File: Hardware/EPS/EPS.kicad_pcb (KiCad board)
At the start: 4 copper layers, 85 x 85 mm, 111 parts, among them J1001 Conn_01x02, J1101 Conn_01x02, J201 Conn_ARM_JTAG_SWD_10, J301 Conn_02x02_Counter_Clockwise, J401 USB_C_Receptacle_PowerOnly_6P, J601 Conn_02x20_Odd_Even, J701 Conn_01x02, J801 Conn_01x02, J901 Conn_01x02, M1201 MountingHole_Pad, M1202 MountingHole_Pad, M1203 MountingHole_Pad, M1204 MountingHole_Pad, Q301 2N7002, U1001 LSM115JE3_TR13, U201 STM32L431RCT, U202 HZ0805E601R-10, U301 RQ3G100GNTB, U302 LTC4162EUFD-L41#PBF, U401 NCP176AMX330TCG, U501 TPS27081ADDCR, U502 RT8258GE, U503 B230A-13-F, U601 PESD3V3L4BHCYL, U602 PESD3V3L4BHCYL, U603 PESD3V3L4BHCYL, U701 LSM115JE3_TR13, U801 LSM115JE3_TR13, U901 LSM115JE3_TR13

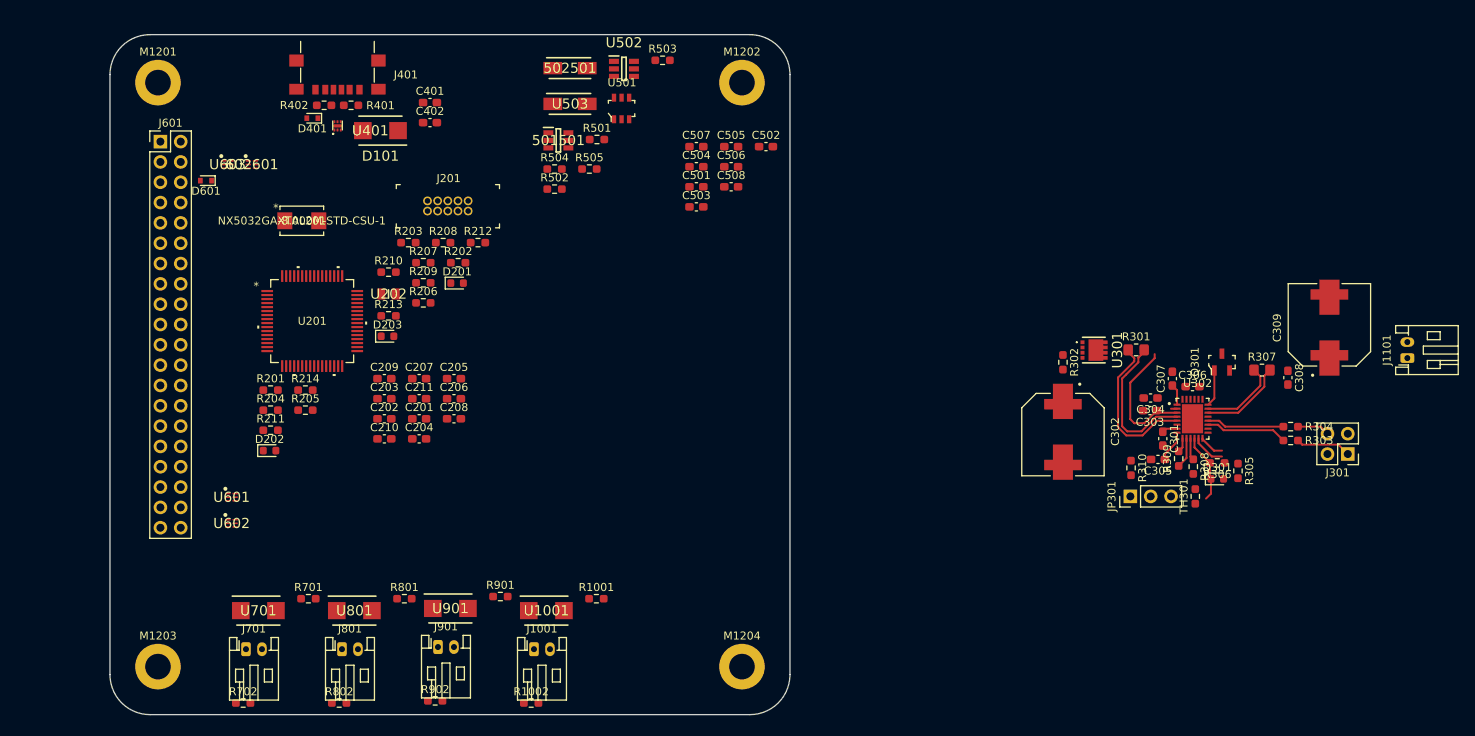
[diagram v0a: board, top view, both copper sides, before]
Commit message: MPPT & Power layout finished
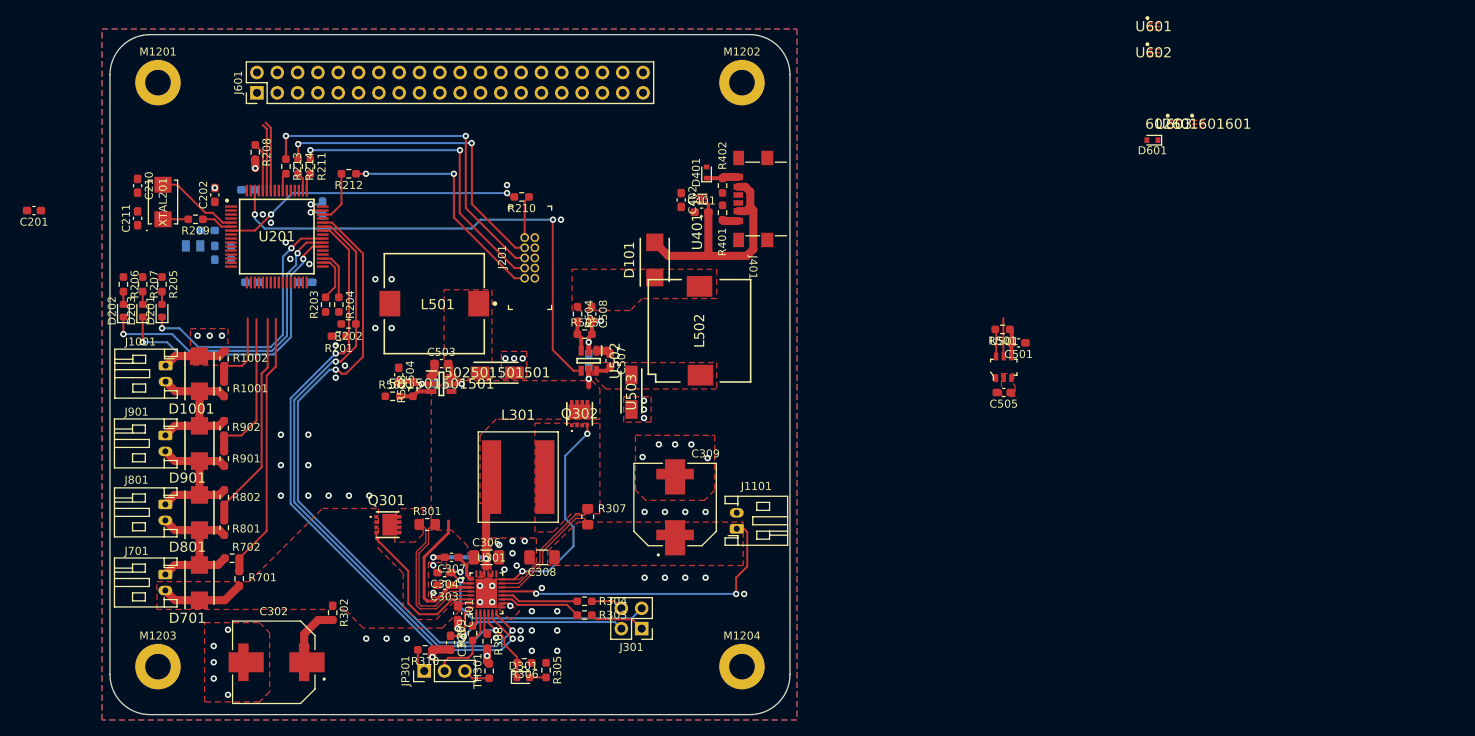
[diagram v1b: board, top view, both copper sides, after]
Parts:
- removed the Q301 at (248.1, 101.3)
- added G001: LOGO, LOGO, B.Cu at (130.3, 136.9)
- added L301: 4.7uH, XAL1060-222MEB:XAL1060222MEB, F.Cu at (160.1, 115.7)
- added L501: 10uH, SLF12555T-100M3R4-PF:SLF12555T, F.Cu at (149.6, 94.0)
- added L502: 15uH, SLF12565T-150M4R2-PF:SLF12565, F.Cu at (182.8, 97.4)
- added Q302: RQ3G100GNTB, RQ3G100GNTB:RQ3G100GNTB, F.Cu at (167.8, 107.7)
- C203, C204, C205, C206, C207, C208, C209, C502, C506, U202: moved to B.Cu
- C306, C308: footprint Capacitor_SMD:C_0603_1608Metric_Pad1.08x0.95mm_HandSolder -> Capacitor_SMD:C_1206_3216Metric_Pad1.33x1.80mm_HandSolder
- U201: footprint STM32L431RCT:LQFP-64 -> STM32L431RCT6:QFP50P1200X1200X160-64N
- XTAL201: footprint footprints:NX5032GA-8.000M-STD-CSU-1 -> NX5032GA-8.000M:XTAL_NX5032_NDK-M
- moved U601 129.4 mm to (239.5, 59.3)
- moved U602 129.4 mm to (239.5, 62.6)
- moved 602601601601 118.4 mm to (245.1, 71.5)
- moved D601 118.4 mm to (239.4, 73.5)
- moved U603 118.4 mm to (242.1, 71.5)
- moved C302 102.7 mm to (129.5, 138.8), turned to 180 degrees
- moved R302 96.5 mm to (136.9, 132.6)
- moved C308 95.9 mm to (163.1, 125.7), turned to 180 degrees
- moved C307 92.8 mm to (151.8, 125.7), turned to 180 degrees
- moved C305 91.3 mm to (151.6, 136.4), turned to -90 degrees
- moved R301 91.3 mm to (148.7, 121.6)
- moved R310 91.1 mm to (148.5, 137.3), turned to 180 degrees
- moved JP301 90.9 mm to (148.4, 139.9)
- moved R309 90.9 mm to (154.4, 135.2)
- moved TH301 90.9 mm to (156.5, 139.9)
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- renumbered 501501 to 501501501501, 502501 to 502501501501, 602601 to 602601601601, U1001 to D1001, U701 to D701, U801 to D801, U901 to D901, U301 to Q301, U302 to U301
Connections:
- 602601601601 pad 3: /GPIO_0 -> unconnected-(602601601601-Pad3)
- 602601601601 pad 4: /GPIO_5 -> unconnected-(602601601601-Pad4)
- 602601601601 pad 6: /SPI_MOSI -> unconnected-(602601601601-Pad6)
- J401 pad S1: GND -> unconnected-(J401-PadS1)
- J601 pad 10: GND -> /PWM_4
- J601 pad 11: GND -> /SPI_MISO
- J601 pad 12: /PWM_4 -> unconnected-(J601-Pad12)
- J601 pad 13: /GPIO_5 -> /SPI_SCK
- J601 pad 15: GND -> unconnected-(J601-Pad15)
- J601 pad 17: /SPI_MOSI -> /Board Connector/3.3V_PIN
- J601 pad 18: GND -> /SDA_CONN
- J601 pad 19: GND -> unconnected-(J601-Pad19)
- J601 pad 20: /SDA_CONN -> GND
- J601 pad 21: /SPI_MISO -> unconnected-(J601-Pad21)
- J601 pad 22: GND -> /SERIAL1_TX
- J601 pad 23: GND -> /SERIAL_RX
- J601 pad 24: /SERIAL1_TX -> unconnected-(J601-Pad24)
- J601 pad 25: /SPI_SCK -> GND
- J601 pad 26: GND -> unconnected-(J601-Pad26)
- J601 pad 27: GND -> unconnected-(J601-Pad27)
- J601 pad 29: /SERIAL_RX -> unconnected-(J601-Pad29)
- J601 pad 3: /Board Connector/3.3V_PIN -> /GPIO_0
- J601 pad 31: GND -> unconnected-(J601-Pad31)
- J601 pad 33: /SERIAL_TX -> unconnected-(J601-Pad33)
- J601 pad 35: GND -> unconnected-(J601-Pad35)
- J601 pad 37: GND -> /SERIAL_TX
- J601 pad 38: GND -> unconnected-(J601-Pad38)
- J601 pad 40: GND -> unconnected-(J601-Pad40)
- J601 pad 5: /Board Connector/3.3V_PIN -> /GPIO_5
- J601 pad 7: GND -> /SPI_MOSI
- J601 pad 9: /GPIO_0 -> GND
- U601 pad 1: /PWM_3 -> unconnected-(U601-Pad1)
- U601 pad 3: /PWM_4 -> unconnected-(U601-Pad3)
- U601 pad 4: /SCL_CONN -> unconnected-(U601-Pad4)
- U601 pad 6: /SDA_CONN -> unconnected-(U601-Pad6)
- U602 pad 1: /SPI_MISO -> unconnected-(U602-Pad1)
- U602 pad 3: /SPI_SCK -> unconnected-(U602-Pad3)
- U602 pad 4: /SERIAL_RX -> unconnected-(U602-Pad4)
- U602 pad 6: /SERIAL_TX -> unconnected-(U602-Pad6)
- U603 pad 1: /SERIAL1_TX -> unconnected-(U603-Pad1)
- U603 pad 3: /SERIAL1_RX -> unconnected-(U603-Pad3)
- U603 pad 4: /PWM_1 -> unconnected-(U603-Pad4)
- U603 pad 6: /PWM_2 -> unconnected-(U603-Pad6)
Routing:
- net /ALERT_MPPT: track 8.66 -> 85.2 mm, vias 0 -> 2
- net /SDA_MPPT: track 3.14 -> 79.2 mm, vias 0 -> 2
- net /SCL_MPPT: track 4.24 -> 79.9 mm, vias 0 -> 2
- net /5V0_ENABLE: track 0.00 -> 62.7 mm, vias 0 -> 2
- net Net-(J201-Pad6): track 0.00 -> 44.3 mm, vias 0 -> 2
- net /Battery_Connector/VBAT: track 10.8 -> 54.9 mm, vias 0 -> 2
- net Net-(J201-Pad8): track 0.00 -> 40.1 mm, vias 0 -> 2
- net /STM32 MCU/LED_G: track 0.00 -> 38.9 mm, vias 0 -> 2
- net Net-(J201-Pad4): track 0.00 -> 38.7 mm, vias 0 -> 2
- net GND: track 0.00 -> 38.1 mm, vias 0 -> 57
- net /STM32 MCU/NRST: track 0.00 -> 37.6 mm, vias 0 -> 2
- net /STM32 MCU/LED_YL: track 0.00 -> 36.9 mm, vias 0 -> 2
- net /STM32 MCU/LED_R: track 0.00 -> 33.8 mm, vias 0 -> 2
- net /STM32 MCU/ADC1: track 0.00 -> 33.4 mm
- net /USB Power/USB_VBUS: track 0.00 -> 31.0 mm
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- added copper zone on B.Cu, net +3.3V
- added copper zone on F.Cu, net +3.3V
- added copper zone on F.Cu, net +5V
- added copper zone on F.Cu, net /Battery_Connector/VBAT
- added copper zone on F.Cu, net /Board Connector/3.3V_PIN
- added copper zone on F.Cu, net /MPPT DC-DC/VIN
- added copper zone on F.Cu, net /MPPT DC-DC/VOUT
- added copper zone on F.Cu, net GND
- added copper zone on In1.Cu, net GND
- added copper zone on In2.Cu, net GND
- added copper zone on F.Cu, net Net-(501501501501-Pad6)
- added copper zone on F.Cu, net Net-(C307-Pad2)
- added copper zone on F.Cu, net Net-(C507-Pad2)
- added copper zone on F.Cu, net Net-(L301-Pad2)
- added copper zone on F.Cu, net Net-(Q301-Pad5)

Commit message: Changed uC pinout and finished uC routing
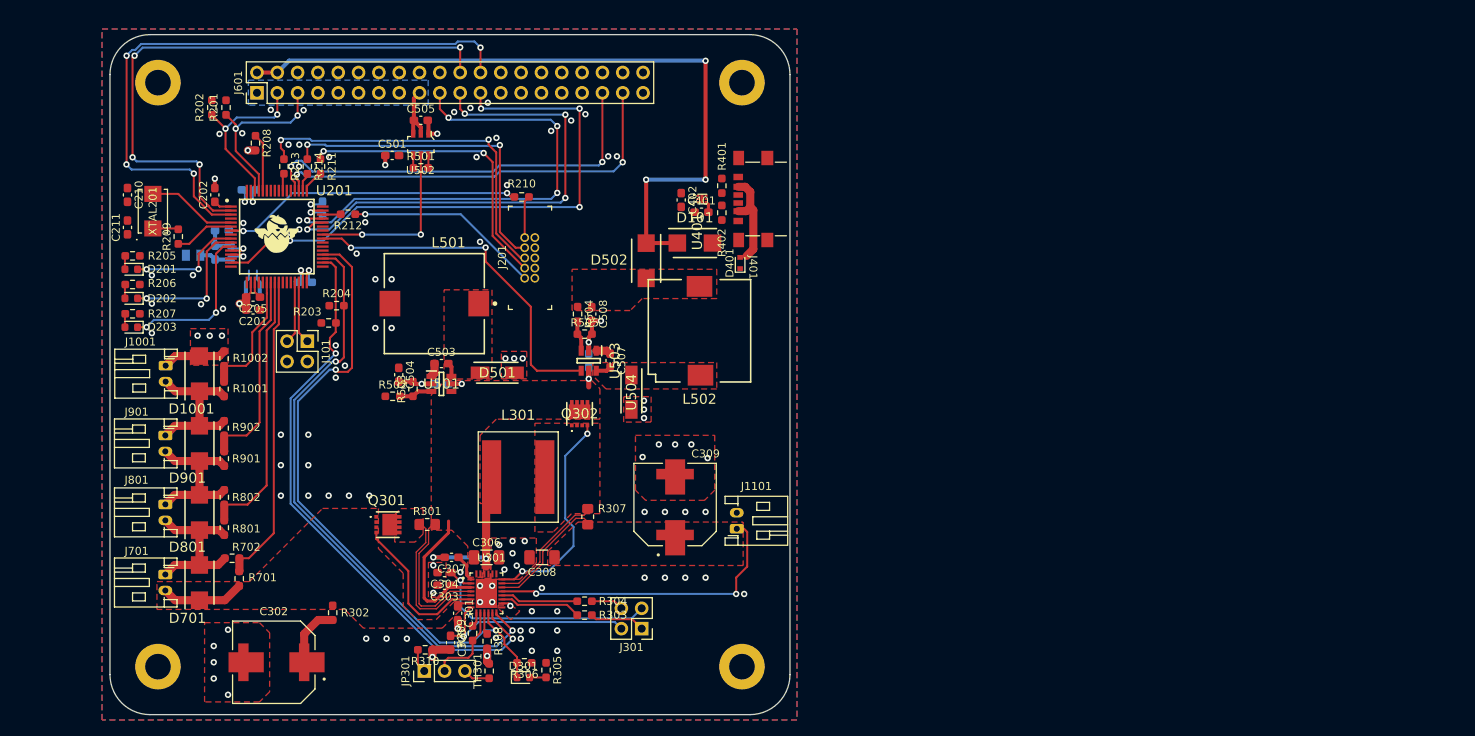
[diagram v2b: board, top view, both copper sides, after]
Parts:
- removed 602601601601, U601, U602, U603: PESD3V3L4BHCYL, PESD3V3L4BHCYL:SON45P80X130X43-6N
- removed D601: PESD5V0S1BB_115, Diode_SMD:D_SOD-523
- added D502: LSM115JE3_TR13, LSM115JE3_TR13:DIOM5436X330N, F.Cu at (176.1, 88.6)
- added G002: LOGO, LOGO, F.Cu at (129.4, 85.4)
- added G003: LOGO, LOGO, B.Cu at (160.1, 115.0)
- added J101: Conn_02x02_Odd_Even, Connector_PinHeader_2.54mm:PinHeader_2x02_P2.54mm_Vertical, F.Cu at (133.7, 98.7)
- C205: moved to F.Cu
- moved C501 81.7 mm to (144.3, 75.5), turned to 0 degrees
- moved C505 80.4 mm to (147.9, 71.1), turned to 0 degrees
- moved U502 78.0 mm to (147.9, 74.1), turned to 180 degrees
- moved R501 75.5 mm to (147.9, 77.0), turned to 0 degrees
- moved G001 69.7 mm to (179.6, 87.6)
- moved R202 32.0 mm to (121.8, 69.5), turned to 90 degrees
- moved R201 31.9 mm to (123.6, 69.5), turned to -90 degrees
- moved C201 30.1 mm to (126.9, 94.8)
- moved D401 12.1 mm to (187.8, 88.9)
- moved D201 6.45 mm to (111.7, 89.7), turned to 180 degrees
- moved D101 5.45 mm to (182.2, 86.4), turned to 0 degrees
- moved R205 5.12 mm to (111.9, 88.0), turned to 180 degrees
- moved R212 5.06 mm to (138.8, 82.8)
- moved R207 3.90 mm to (111.9, 95.2), turned to 180 degrees
- moved R402 3.39 mm to (185.5, 82.6), turned to -90 degrees
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- renumbered 502501501501 to D501, 501501501501 to U501, U501 to U502, U502 to U503, U503 to U504
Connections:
- C508 pad 1: +5V -> Net-(C508-Pad1)
- J601 pad 10: /PWM_4 -> unconnected-(J601-Pad10)
- J601 pad 11: /SPI_MISO -> unconnected-(J601-Pad11)
- J601 pad 13: /SPI_SCK -> unconnected-(J601-Pad13)
- J601 pad 16: /SCL_CONN -> unconnected-(J601-Pad16)
- J601 pad 18: /SDA_CONN -> unconnected-(J601-Pad18)
- J601 pad 19: unconnected-(J601-Pad19) -> /SPI_MOSI
- J601 pad 21: unconnected-(J601-Pad21) -> /SPI_MISO
- J601 pad 22: /SERIAL1_TX -> /GPIO_13
- J601 pad 23: /SERIAL_RX -> /SPI_SCK
- J601 pad 24: unconnected-(J601-Pad24) -> /GPIO_14
- J601 pad 28: /SERIAL1_RX -> unconnected-(J601-Pad28)
- J601 pad 3: /GPIO_0 -> /SDA_CONN
- J601 pad 32: /PWM_1 -> /Board Connector/PIN_32
- J601 pad 35: unconnected-(J601-Pad35) -> /SERIAL_RX
- J601 pad 36: /PWM_2 -> /Board Connector/PIN_36
- J601 pad 5: /GPIO_5 -> /SCL_CONN
- J601 pad 7: /SPI_MOSI -> unconnected-(J601-Pad7)
- J601 pad 8: /PWM_3 -> unconnected-(J601-Pad8)
- L502 pad 2: +5V -> Net-(C508-Pad1)
- R1001 pad 2: /STM32 MCU/ADC4 -> /STM32 MCU/ADC1
- R1002 pad 2: /STM32 MCU/ADC4 -> /STM32 MCU/ADC1
- R201 pad 2: /SCL_MPPT -> /SCL_CONN
- R202 pad 1: /SDA_MPPT -> /SDA_CONN
- R203 pad 2: /SCL_CONN -> /SCL_MPPT
- R204 pad 1: /SDA_CONN -> /SDA_MPPT
- R504 pad 1: +5V -> Net-(C508-Pad1)
- R701 pad 2: /STM32 MCU/ADC1 -> /STM32 MCU/ADC4
- R702 pad 2: /STM32 MCU/ADC1 -> /STM32 MCU/ADC4
- R801 pad 2: /STM32 MCU/ADC2 -> /STM32 MCU/ADC3
- R802 pad 2: /STM32 MCU/ADC2 -> /STM32 MCU/ADC3
- R901 pad 2: /STM32 MCU/ADC3 -> /STM32 MCU/ADC2
- R902 pad 2: /STM32 MCU/ADC3 -> /STM32 MCU/ADC2
- U201 pad 10: /STM32 MCU/ADC3 -> /STM32 MCU/LED_G
- U201 pad 11: /STM32 MCU/ADC4 -> /STM32 MCU/LED_YL
- U201 pad 14: /PWM_1 -> unconnected-(U201-Pad14)
- U201 pad 15: /PWM_2 -> /SPI_SCK
- U201 pad 16: /SERIAL_TX -> unconnected-(U201-Pad16)
- U201 pad 17: /SERIAL_RX -> unconnected-(U201-Pad17)
- U201 pad 2: unconnected-(U201-Pad2) -> /GPIO_13
- U201 pad 21: /SPI_SCK -> unconnected-(U201-Pad21)
- U201 pad 22: /SPI_MISO -> /STM32 MCU/ADC1
- U201 pad 23: /SPI_MOSI -> /STM32 MCU/ADC2
- U201 pad 24: unconnected-(U201-Pad24) -> /STM32 MCU/ADC3
- U201 pad 25: /GPIO_5 -> /STM32 MCU/ADC4
- U201 pad 26: /GPIO_0 -> unconnected-(U201-Pad26)
- U201 pad 29: /PWM_3 -> /STM32 MCU/PWM_CH3
- U201 pad 3: unconnected-(U201-Pad3) -> /GPIO_14
- U201 pad 30: /PWM_4 -> /STM32 MCU/PWM_CH4
- U201 pad 34: /SCL_CONN -> /SCL_MPPT
- U201 pad 35: /SDA_CONN -> /SDA_MPPT
- U201 pad 36: unconnected-(U201-Pad36) -> /ALERT_MPPT
- U201 pad 38: /STM32 MCU/LED_YL -> unconnected-(U201-Pad38)
- U201 pad 39: /STM32 MCU/LED_G -> unconnected-(U201-Pad39)
- U201 pad 40: /STM32 MCU/LED_R -> /5V0_ENABLE
- U201 pad 41: unconnected-(U201-Pad41) -> /3V3_ENABLE
- U201 pad 42: /SCL_MPPT -> unconnected-(U201-Pad42)
- U201 pad 43: /SDA_MPPT -> unconnected-(U201-Pad43)
- U201 pad 44: /ALERT_MPPT -> /SPI_MISO
- U201 pad 45: unconnected-(U201-Pad45) -> /SPI_MOSI
- U201 pad 51: unconnected-(U201-Pad51) -> /SERIAL_TX
- U201 pad 52: unconnected-(U201-Pad52) -> /SERIAL_RX
- U201 pad 58: /SERIAL1_TX -> unconnected-(U201-Pad58)
- U201 pad 59: /SERIAL1_RX -> unconnected-(U201-Pad59)
- U201 pad 61: /3V3_ENABLE -> /SCL_CONN
- U201 pad 62: /5V0_ENABLE -> /SDA_CONN
- U201 pad 8: /STM32 MCU/ADC1 -> unconnected-(U201-Pad8)
- U201 pad 9: /STM32 MCU/ADC2 -> /STM32 MCU/LED_R
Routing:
- net +5V: track 0.00 -> 90.8 mm, vias 0 -> 3
- net /GPIO_14: track 0.00 -> 79.4 mm, vias 0 -> 4
- net /GPIO_13: track 0.00 -> 74.5 mm, vias 0 -> 4
- net /SPI_SCK: track 0.00 -> 73.1 mm, vias 0 -> 4
- net /SPI_MISO: track 0.00 -> 62.1 mm, vias 0 -> 4
- net /SPI_MOSI: track 0.00 -> 60.9 mm, vias 0 -> 4
- net /SERIAL_TX: track 0.00 -> 52.6 mm, vias 0 -> 2
- net /SERIAL_RX: track 0.00 -> 52.2 mm, vias 0 -> 2
- net /STM32 MCU/ADC4: track 10.5 -> 38.8 mm
- net GND: track 38.1 -> 59.8 mm, vias 57 -> 88
- net /STM32 MCU/LED_G: track 38.9 -> 18.0 mm
- net /STM32 MCU/LED_R: track 33.8 -> 14.4 mm
- net /5V0_ENABLE: track 62.7 -> 44.4 mm
- net /USB Power/USB_VBUS: track 31.0 -> 13.3 mm
- net /3V3_ENABLE: track 4.82 -> 22.2 mm, vias 0 -> 2
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- added copper zone on B.Cu, net /Board Connector/3.3V_PIN
- added copper zone on F.Cu, net Net-(C508-Pad1)
- removed copper zone on F.Cu, net +5V
- removed copper zone on F.Cu, net /Board Connector/3.3V_PIN
